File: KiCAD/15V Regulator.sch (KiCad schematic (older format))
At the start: 33 parts, among them U36 ADP5070AREZ

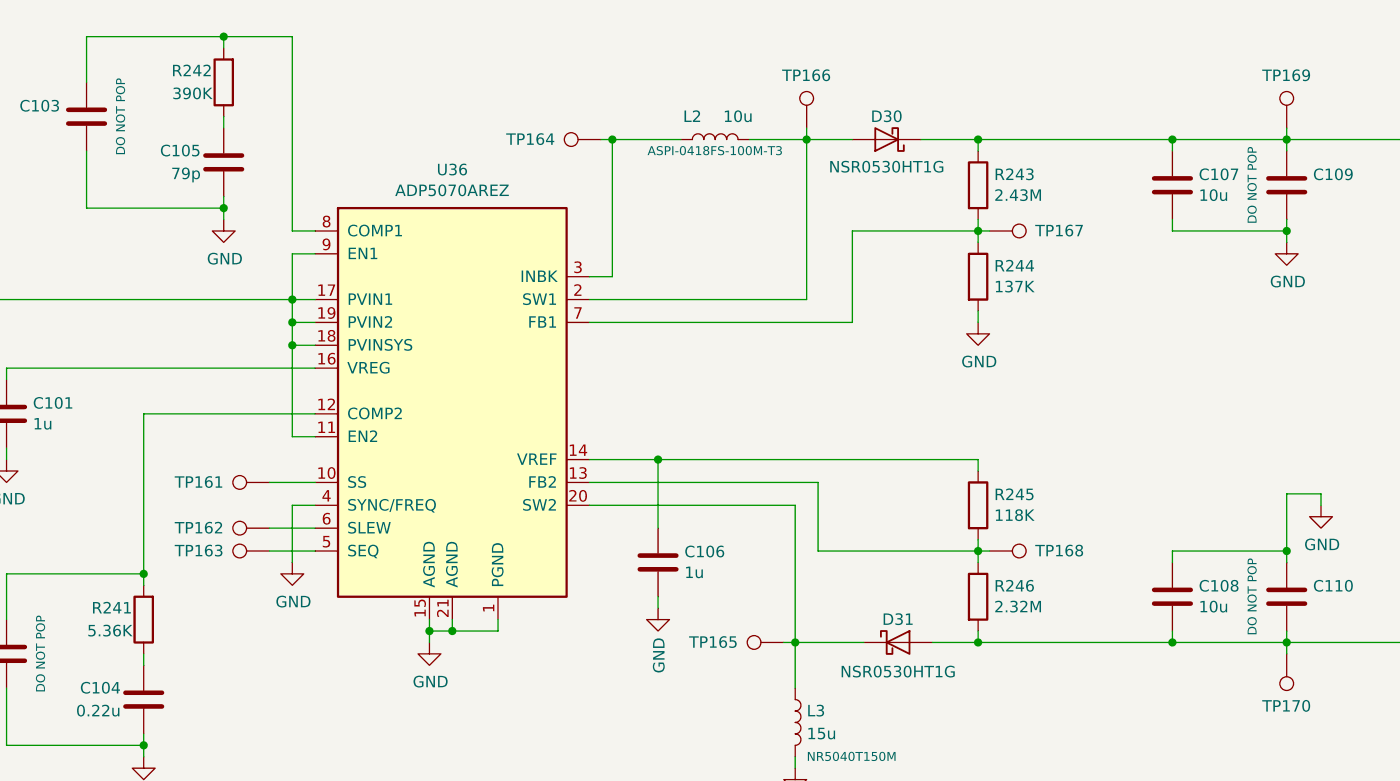
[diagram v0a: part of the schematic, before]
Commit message: Add power changeover circuit, fix minor issues
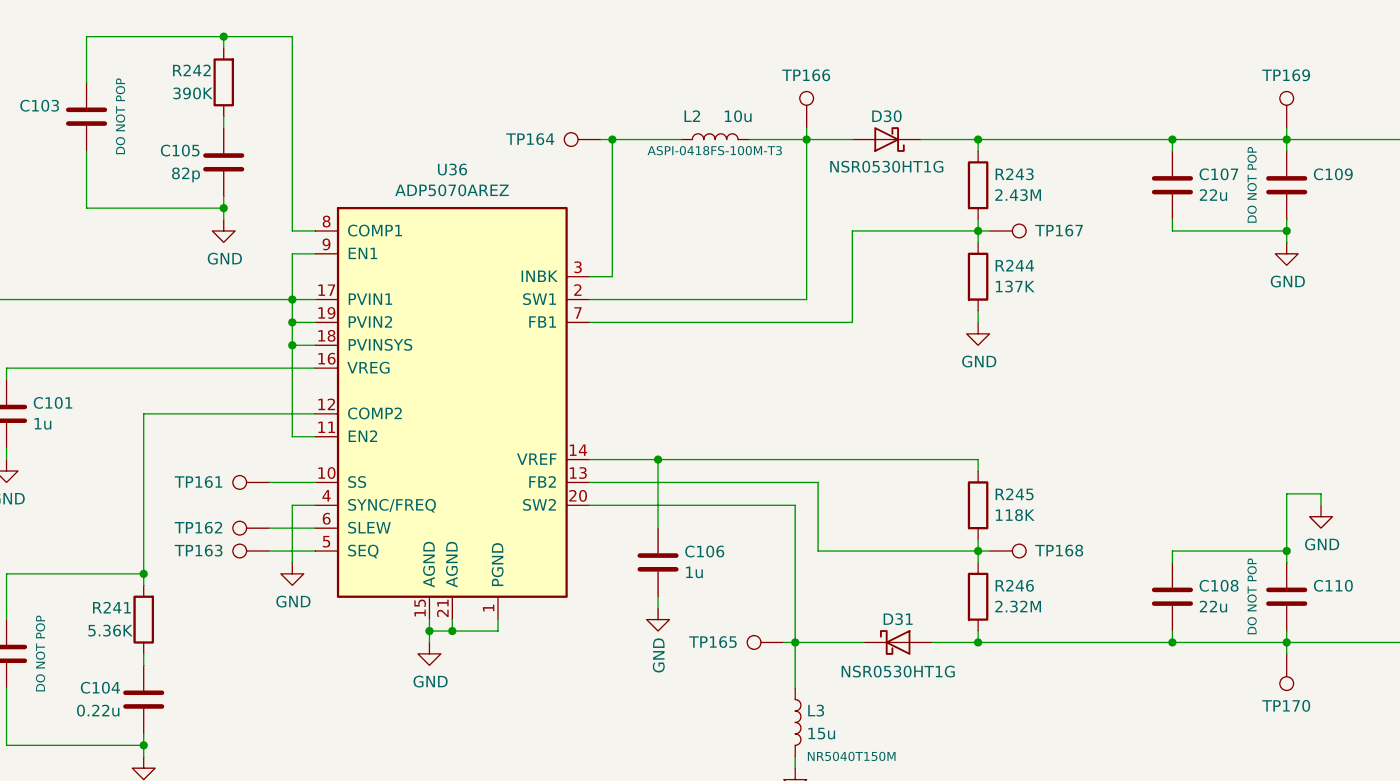
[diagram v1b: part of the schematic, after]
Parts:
- C105: value 79p -> 82p
- C107, C108: value 10u -> 22u
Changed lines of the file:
@@
 Sheet 9 10
 Title "+/-15V REGULATOR"
-Date "2020-02-03"
+Date "2020-02-04"
 Rev "A"
 Comp "THE UNIVERSITY OF AKRON"
@@
 P 6850 3900
 F 0 "C105" H 6950 3850 50  0000 L CNN
-F 1 "79p" H 6950 3950 50  0000 L CNN
+F 1 "82p" H 6950 3950 50  0000 L CNN
 F 2 "Capacitor_SMD:C_0603_1608Metric" H 6888 3750 50  0001 C CNN
 F 3 "~" H 6850 3900 50  0001 C CNN
@@
 P 11000 4000
 F 0 "C107" H 11115 4046 50  0000 L CNN
-F 1 "10u" H 11115 3955 50  0000 L CNN
+F 1 "22u" H 11115 3955 50  0000 L CNN
 F 2 "Capacitor_SMD:C_1206_3216Metric" H 11038 3850 50  0001 C CNN
 F 3 "~" H 11000 4000 50  0001 C CNN
@@
 P 11000 5800
 F 0 "C108" H 11115 5846 50  0000 L CNN
-F 1 "10u" H 11115 5755 50  0000 L CNN
+F 1 "22u" H 11115 5755 50  0000 L CNN
 F 2 "Capacitor_SMD:C_1206_3216Metric" H 11038 5650 50  0001 C CNN
 F 3 "~" H 11000 5800 50  0001 C CNN

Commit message: Assign footprints, fix minor schematic issues
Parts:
- C100: footprint Capacitor_SMD:C_1206_3216Metric -> Capacitor_SMD:C_0805_2012Metric
- C101, C106: footprint Capacitor_SMD:C_1206_3216Metric -> Capacitor_SMD:C_0603_1608Metric
- C107, C108, C99: footprint Capacitor_SMD:C_1206_3216Metric -> Capacitor_SMD:C_1210_3225Metric
- C109, C110: footprint Capacitor_SMD:C_0603_1608Metric -> Capacitor_SMD:C_1210_3225Metric
- L2: footprint io_master:L_Murata_DEM80xxC -> io-master:L_Abracon_ASPI-0418FS
- L3: footprint io_master:L_Murata_DEM80xxC -> Inductor_SMD:L_Taiyo-Yuden_NR-50xx
- TP161, TP162, TP163, TP164, TP165, TP166, TP167, TP168: footprint TestPoint:TestPoint_THTPad_D1.0mm_Drill0.5mm -> TestPoint:TestPoint_Pad_D1.0mm
- TP169: value +24V -> +15V; footprint TestPoint:TestPoint_THTPad_D1.0mm_Drill0.5mm -> TestPoint:TestPoint_Pad_D1.0mm
- TP170: value -24V -> -15V; footprint TestPoint:TestPoint_THTPad_D1.0mm_Drill0.5mm -> TestPoint:TestPoint_Pad_D1.0mm
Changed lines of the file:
@@
 F 0 "L2" V 9100 3900 50  0000 C CNN
 F 1 "10u" V 9100 3700 50  0000 C CNN
-F 2 "io_master:L_Murata_DEM80xxC" H 9000 3800 50  0001 C CNN
+F 2 "io-master:L_Abracon_ASPI-0418FS" H 9000 3800 50  0001 C CNN
 F 3 "~" H 9000 3800 50  0001 C CNN
 F 4 "ASPI-0418FS-100M-T3" V 8950 3800 39  0000 C CNN "Device"
@@
 F 0 "C106" H 8865 5696 50  0000 L CNN
 F 1 "1u" H 8865 5605 50  0000 L CNN
-F 2 "Capacitor_SMD:C_1206_3216Metric" H 8788 5500 50  0001 C CNN
+F 2 "Capacitor_SMD:C_0603_1608Metric" H 8788 5500 50  0001 C CNN
 F 3 "~" H 8750 5650 50  0001 C CNN
 	1    8750 5650
@@
 F 0 "L3" H 9400 6400 50  0000 L CNN
 F 1 "15u" H 9400 6300 50  0000 L CNN
-F 2 "io_master:L_Murata_DEM80xxC" H 9350 6350 50  0001 C CNN
+F 2 "Inductor_SMD:L_Taiyo-Yuden_NR-50xx" H 9350 6350 50  0001 C CNN
 F 3 "~" H 9350 6350 50  0001 C CNN
 F 4 "NR5040T150M" H 9400 6200 39  0000 L CNN "Device"
@@
 F 0 "TP161" V 7050 5500 50  0000 L CNN
 F 1 "SS" H 7108 5327 50  0001 L CNN
-F 2 "TestPoint:TestPoint_THTPad_D1.0mm_Drill0.5mm" H 7250 5300 50  0001 C CNN
+F 2 "TestPoint:TestPoint_Pad_D1.0mm" H 7250 5300 50  0001 C CNN
 F 3 "~" H 7250 5300 50  0001 C CNN
 	1    7050 5300
@@
 $EndComp
 $Comp
-L Connector:TestPoint TP162
-U 1 1 5DD030EA
-P 7050 5500
-F 0 "TP162" V 7050 5700 50  0000 L CNN
-F 1 "SLEW" H 7108 5527 50  0001 L CNN
-F 2 "TestPoint:TestPoint_THTPad_D1.0mm_Drill0.5mm" H 7250 5500 50  0001 C CNN
-F 3 "~" H 7250 5500 50  0001 C CNN
-	1    7050 5500
-	0    -1   -1   0
-$EndComp
-$Comp
 L Connector:TestPoint TP163
 U 1 1 5DD03411
@@
 F 0 "TP163" V 7050 5800 50  0000 L CNN
 F 1 "SEQ" H 7108 5627 50  0001 L CNN
-F 2 "TestPoint:TestPoint_THTPad_D1.0mm_Drill0.5mm" H 7250 5600 50  0001 C CNN
+F 2 "TestPoint:TestPoint_Pad_D1.0mm" H 7250 5600 50  0001 C CNN
 F 3 "~" H 7250 5600 50  0001 C CNN
 	1    7050 5600
@@
 F 0 "C109" H 11615 4046 50  0000 L CNN
 F 1 "C" H 11615 3955 50  0001 L CNN
-F 2 "Capacitor_SMD:C_0603_1608Metric" H 11538 3850 50  0001 C CNN
+F 2 "Capacitor_SMD:C_1210_3225Metric" H 11538 3850 50  0001 C CNN
 F 3 "~" H 11500 4000 50  0001 C CNN
 F 4 "DO NOT POP" V 11350 4000 39  0000 C CNN "Depop"
@@
 F 0 "C110" H 11615 5846 50  0000 L CNN
 F 1 "C" H 11615 5755 50  0001 L CNN
-F 2 "Capacitor_SMD:C_0603_1608Metric" H 11538 5650 50  0001 C CNN
+F 2 "Capacitor_SMD:C_1210_3225Metric" H 11538 5650 50  0001 C CNN
 F 3 "~" H 11500 5800 50  0001 C CNN
 F 4 "DO NOT POP" V 11350 5800 39  0000 C CNN "Depop"
@@
 F 0 "TP164" V 8500 4000 50  0000 L CNN
 F 1 "INBK" H 8558 3827 50  0001 L CNN
-F 2 "TestPoint:TestPoint_THTPad_D1.0mm_Drill0.5mm" H 8700 3800 50  0001 C CNN
+F 2 "TestPoint:TestPoint_Pad_D1.0mm" H 8700 3800 50  0001 C CNN
 F 3 "~" H 8700 3800 50  0001 C CNN
 	1    8500 3800
@@
 F 0 "TP167" V 10200 4400 50  0000 L CNN
 F 1 "FB1" H 10258 4227 50  0001 L CNN
-F 2 "TestPoint:TestPoint_THTPad_D1.0mm_Drill0.5mm" H 10400 4200 50  0001 C CNN
+F 2 "TestPoint:TestPoint_Pad_D1.0mm" H 10400 4200 50  0001 C CNN
 F 3 "~" H 10400 4200 50  0001 C CNN
 	1    10200 4200
@@
 F 0 "TP168" V 10200 5800 50  0000 L CNN
 F 1 "FB2" H 10258 5627 50  0001 L CNN
-F 2 "TestPoint:TestPoint_THTPad_D1.0mm_Drill0.5mm" H 10400 5600 50  0001 C CNN
+F 2 "TestPoint:TestPoint_Pad_D1.0mm" H 10400 5600 50  0001 C CNN
 F 3 "~" H 10400 5600 50  0001 C CNN
 	1    10200 5600
@@
 F 0 "TP166" H 9400 3950 50  0000 C BNN
 F 1 "SW1" H 9458 3777 50  0001 L CNN
-F 2 "TestPoint:TestPoint_THTPad_D1.0mm_Drill0.5mm" H 9600 3750 50  0001 C CNN
+F 2 "TestPoint:TestPoint_Pad_D1.0mm" H 9600 3750 50  0001 C CNN
 F 3 "~" H 9600 3750 50  0001 C CNN
 	1    9400 3750
@@
 F 0 "TP165" V 9300 6200 50  0000 L CNN
 F 1 "SW2" H 9358 6027 50  0001 L CNN
-F 2 "TestPoint:TestPoint_THTPad_D1.0mm_Drill0.5mm" H 9500 6000 50  0001 C CNN
+F 2 "TestPoint:TestPoint_Pad_D1.0mm" H 9500 6000 50  0001 C CNN
 F 3 "~" H 9500 6000 50  0001 C CNN
 	1    9300 6000
@@
 P 11500 3750
 F 0 "TP169" H 11500 3950 50  0000 C BNN
-F 1 "+24V" H 11558 3777 50  0001 L CNN
-F 2 "TestPoint:TestPoint_THTPad_D1.0mm_Drill0.5mm" H 11700 3750 50  0001 C CNN
+F 1 "+15V" H 11558 3777 50  0001 L CNN
+F 2 "TestPoint:TestPoint_Pad_D1.0mm" H 11700 3750 50  0001 C CNN
 F 3 "~" H 11700 3750 50  0001 C CNN
 	1    11500 3750
@@
 P 11500 6050
 F 0 "TP170" H 11500 6250 50  0000 C BNN
-F 1 "-24V" H 11558 6077 50  0001 L CNN
-F 2 "TestPoint:TestPoint_THTPad_D1.0mm_Drill0.5mm" H 11700 6050 50  0001 C CNN
+F 1 "-15V" H 11558 6077 50  0001 L CNN
+F 2 "TestPoint:TestPoint_Pad_D1.0mm" H 11700 6050 50  0001 C CNN
 F 3 "~" H 11700 6050 50  0001 C CNN
 	1    11500 6050
@@
 F 0 "C101" H 6015 5046 50  0000 L CNN
 F 1 "1u" H 6015 4955 50  0000 L CNN
-F 2 "Capacitor_SMD:C_1206_3216Metric" H 5938 4850 50  0001 C CNN
+F 2 "Capacitor_SMD:C_0603_1608Metric" H 5938 4850 50  0001 C CNN
 F 3 "~" H 5900 5000 50  0001 C CNN
 	1    5900 5000
@@
 F 0 "C100" H 5365 4746 50  0000 L CNN
 F 1 "10u" H 5365 4655 50  0000 L CNN
-F 2 "Capacitor_SMD:C_1206_3216Metric" H 5288 4550 50  0001 C CNN
+F 2 "Capacitor_SMD:C_0805_2012Metric" H 5288 4550 50  0001 C CNN
 F 3 "~" H 5250 4700 50  0001 C CNN
 	1    5250 4700
@@
 F 0 "C99" H 4965 4746 50  0000 L CNN
 F 1 "C" H 4965 4655 50  0001 L CNN
-F 2 "Capacitor_SMD:C_1206_3216Metric" H 4888 4550 50  0001 C CNN
+F 2 "Capacitor_SMD:C_1210_3225Metric" H 4888 4550 50  0001 C CNN
 F 3 "~" H 4850 4700 50  0001 C CNN
 F 4 "DO NOT POP" V 4700 4700 39  0000 C CNN "Depop"
@@
 F 0 "C107" H 11115 4046 50  0000 L CNN
 F 1 "22u" H 11115 3955 50  0000 L CNN
-F 2 "Capacitor_SMD:C_1206_3216Metric" H 11038 3850 50  0001 C CNN
+F 2 "Capacitor_SMD:C_1210_3225Metric" H 11038 3850 50  0001 C CNN
 F 3 "~" H 11000 4000 50  0001 C CNN
 	1    11000 4000
@@
 F 0 "C108" H 11115 5846 50  0000 L CNN
 F 1 "22u" H 11115 5755 50  0000 L CNN
-F 2 "Capacitor_SMD:C_1206_3216Metric" H 11038 5650 50  0001 C CNN
+F 2 "Capacitor_SMD:C_1210_3225Metric" H 11038 5650 50  0001 C CNN
 F 3 "~" H 11000 5800 50  0001 C CNN
 	1    11000 5800
@@
 Text Notes 1350 7750 0    50   ~ 0
 RECOMMENDED PCB LAYOUT
+$Comp
+L Connector:TestPoint TP162
+U 1 1 5DD030EA
+P 7050 5500
+F 0 "TP162" V 7050 5700 50  0000 L CNN
+F 1 "SLEW" H 7108 5527 50  0001 L CNN
+F 2 "TestPoint:TestPoint_Pad_D1.0mm" H 7250 5500 50  0001 C CNN
+F 3 "~" H 7250 5500 50  0001 C CNN
+	1    7050 5500
+	0    -1   -1   0
+$EndComp
 $EndSCHEMATC
